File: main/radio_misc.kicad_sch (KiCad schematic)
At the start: 23 parts, among them J1301 Transponder, J1302 Conn_01x03, J1303 Conn_01x03, J1304 Conn_01x03, J1305 Conn_01x03, J1306 Conn_01x03, J1307 Conn_01x03, J1308 USB_B_Micro, M1301 Servo direction, Q1301 IRLML0030, U1301 FT230XQ

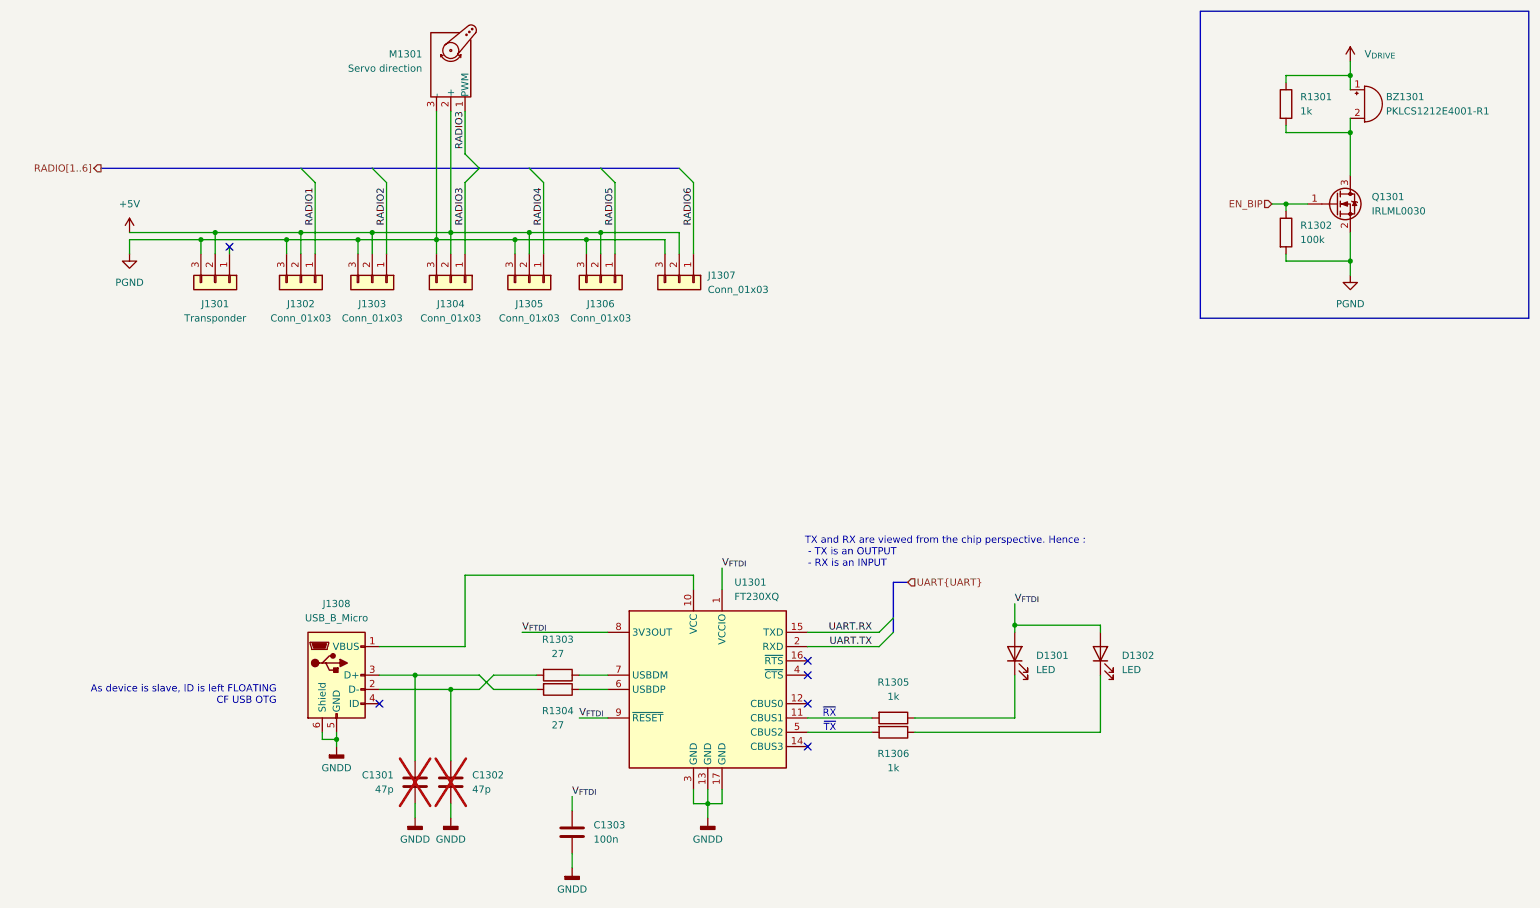
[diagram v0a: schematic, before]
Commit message: Clean silkscreen
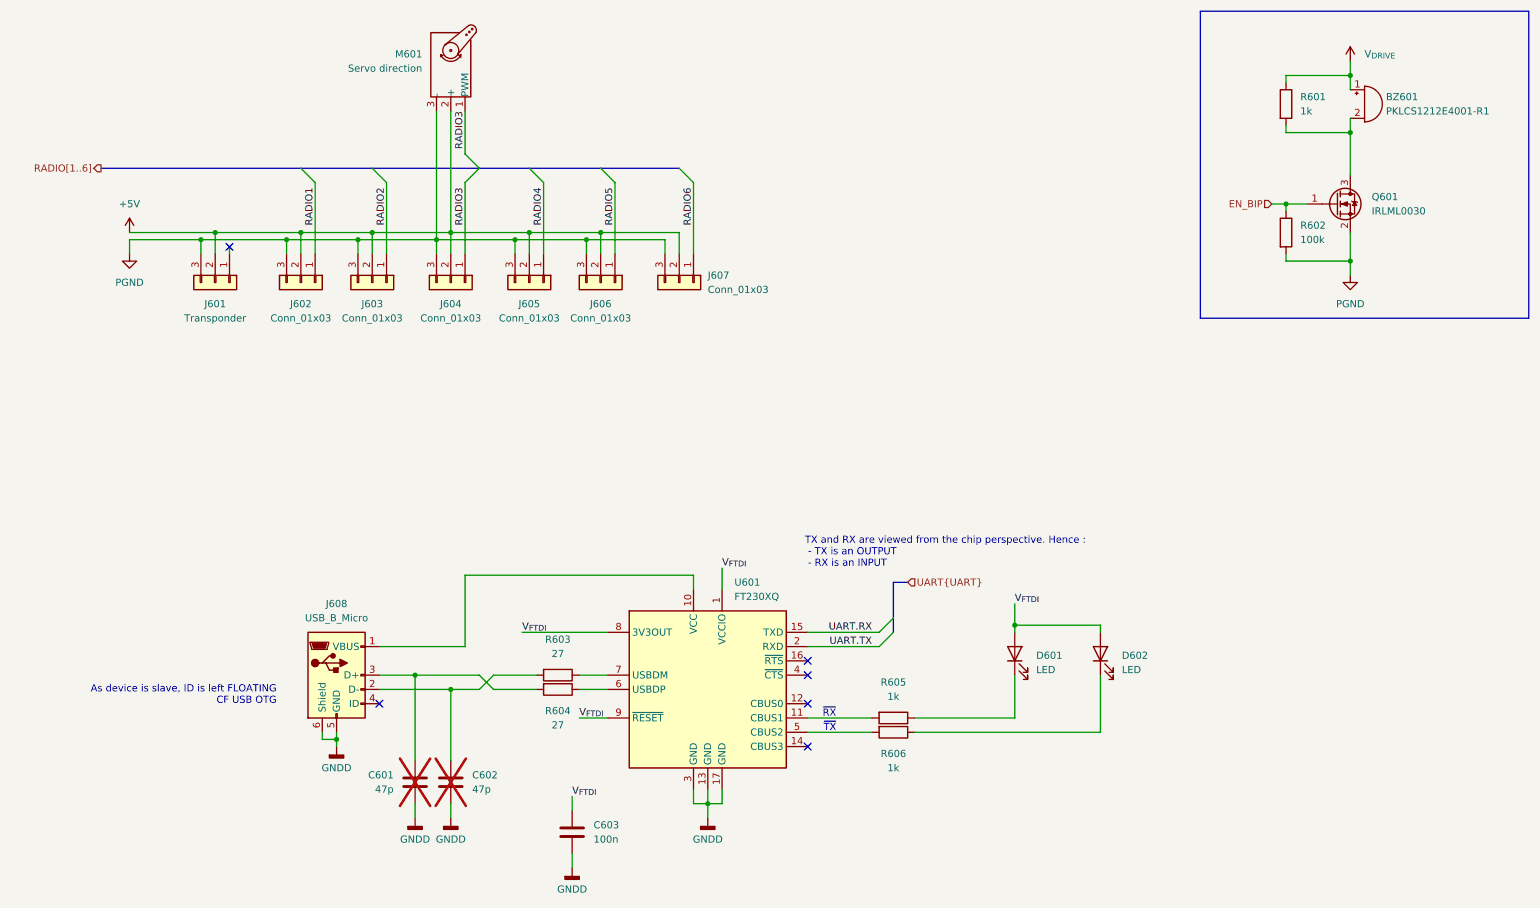
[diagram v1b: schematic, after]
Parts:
- renumbered BZ1301 to BZ601, C1301 to C601, C1302 to C602, C1303 to C603, D1301 to D601, D1302 to D602, J1301 to J601, J1302 to J602, J1303 to J603, J1304 to J604, J1305 to J605, J1306 to J606, J1307 to J607, J1308 to J608, M1301 to M601, Q1301 to Q601, R1301 to R601, R1302 to R602, R1303 to R603, R1304 to R604, R1305 to R605, R1306 to R606, U1301 to U601

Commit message: Sent to fab
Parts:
- C603: MPN (none) -> CL21B104KACNFNC; Mouser SKU (none) -> 187-CL21B104KACNFNC
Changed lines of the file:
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@@
+			)
+		)
+		(property "Quantity" ""
+			(at 240.03 29.21 0)
+			(effects
+				(font
+					(size 1.27 1.27)
+				)
 			)
 		)
@@
 			)
 		)
+		(property "Quantity" ""
+			(at 132.08 60.96 0)
+			(effects
+				(font
+					(size 1.27 1.27)
+				)
+			)
+		)
 		(pin "3"
 		)
@@
 			)
 		)
+		(property "Quantity" ""
+			(at 105.41 60.96 0)
+			(effects
+				(font
+					(size 1.27 1.27)
+				)
+			)
+		)
 		(pin "3"
 		)
@@
 			)
 		)
+		(property "MPN" "CL21B104KACNFNC "
+			(at 113.03 158.75 0)
+			(effects
+				(font
+					(size 1.27 1.27)
+				)
+			)
+		)
+		(property "Mouser SKU" " 187-CL21B104KACNFNC "
+			(at 113.03 158.75 0)
+			(effects
+				(font
+					(size 1.27 1.27)
+				)
+			)
+		)
+		(property "Quantity" ""
+			(at 113.03 158.75 0)
+			(effects
+				(font
+					(size 1.27 1.27)
+				)
+			)
+		)
 		(pin "1"
 		)
@@
 			)
 		)
+		(property "Quantity" ""
+			(at 77.47 60.96 0)
+			(effects
+				(font
+					(size 1.27 1.27)
+				)
+			)
+		)
 		(pin "3"
 		)
@@
 			)
 		)
+		(property "Quantity" ""
+			(at 110.49 133.35 0)
+			(effects
+				(font
+					(size 1.27 1.27)
+				)
+			)
+		)
 		(pin "2"
 		)
@@
 			)
 		)
+		(property "Quantity" ""
+			(at 170.18 138.43 0)
+			(effects
+				(font
+					(size 1.27 1.27)
+				)
+			)
+		)
 		(pin "2"
 		)
@@
 			)
 		)
+		(property "Quantity" ""
+			(at 254 29.21 0)
+			(effects
+				(font
+					(size 1.27 1.27)
+				)
+			)
+		)
 		(pin "2"
 		)
@@
 			)
 		)
+		(property "Quantity" ""
+			(at 248.92 46.99 0)
+			(effects
+				(font
+					(size 1.27 1.27)
+				)
+			)
+		)
 		(pin "3"
 		)
@@
 			)
 		)
+		(property "Quantity" ""
+			(at 64.77 60.96 0)
+			(effects
+				(font
+					(size 1.27 1.27)
+				)
+			)
+		)
 		(pin "3"
 		)
@@
 			)
 		)
+		(property "Quantity" ""
+			(at 137.16 133.35 0)
+			(effects
+				(font
+					(size 1.27 1.27)
+				)
+			)
+		)
 		(pin "17"
 		)
@@
 			)
 		)
+		(property "Quantity" ""
+			(at 91.44 60.96 0)
+			(effects
+				(font
+					(size 1.27 1.27)
+				)
+			)
+		)
 		(pin "3"
 		)
@@
 			)
 		)
+		(property "Quantity" ""
+			(at 170.18 140.97 0)
+			(effects
+				(font
+					(size 1.27 1.27)
+				)
+			)
+		)
 		(pin "2"
 		)
@@
 			)
 		)
+		(property "Quantity" ""
+			(at 118.11 60.96 0)
+			(effects
+				(font
+					(size 1.27 1.27)
+				)
+			)
+		)
 		(pin "3"
 		)
@@
 			)
 		)
+		(property "Quantity" ""
+			(at 110.49 130.81 0)
+			(effects
+				(font
+					(size 1.27 1.27)
+				)
+			)
+		)
 		(pin "2"
 		)
@@
 				)
 				(hide yes)
+			)
+		)
+		(property "Quantity" ""
+			(at 191.77 127 0)
+			(effects
+				(font
+					(size 1.27 1.27)
+				)
 			)
 		)
@@
 			)
 		)
+		(property "Quantity" ""
+			(at 91.44 22.86 0)
+			(effects
+				(font
+					(size 1.27 1.27)
+				)
+			)
+		)
 		(pin "1"
 		)
@@
 			)
 		)
+		(property "Quantity" ""
+			(at 49.53 60.96 0)
+			(effects
+				(font
+					(size 1.27 1.27)
+				)
+			)
+		)
 		(pin "3"
 		)
@@
 			)
 		)
+		(property "Quantity" ""
+			(at 85.09 149.86 0)
+			(effects
+				(font
+					(size 1.27 1.27)
+				)
+			)
+		)
 		(pin "1"
 		)
@@
 			)
 		)
+		(property "Quantity" ""
+			(at 71.12 130.81 0)
+			(effects
+				(font
+					(size 1.27 1.27)
+				)
+			)
+		)
 		(pin "5"
 		)
@@
 			)
 		)
+		(property "Quantity" ""
+			(at 91.44 149.86 0)
+			(effects
+				(font
+					(size 1.27 1.27)
+				)
+			)
+		)
 		(pin "1"
 		)
@@
 			)
 		)
+		(property "Quantity" ""
+			(at 240.03 52.07 0)
+			(effects
+				(font
+					(size 1.27 1.27)
+				)
+			)
+		)
 		(pin "2"
 		)
@@
 			)
 		)
+		(property "Quantity" ""
+			(at 207.01 127 0)
+			(effects
+				(font
+					(size 1.27 1.27)
+				)
+			)
+		)

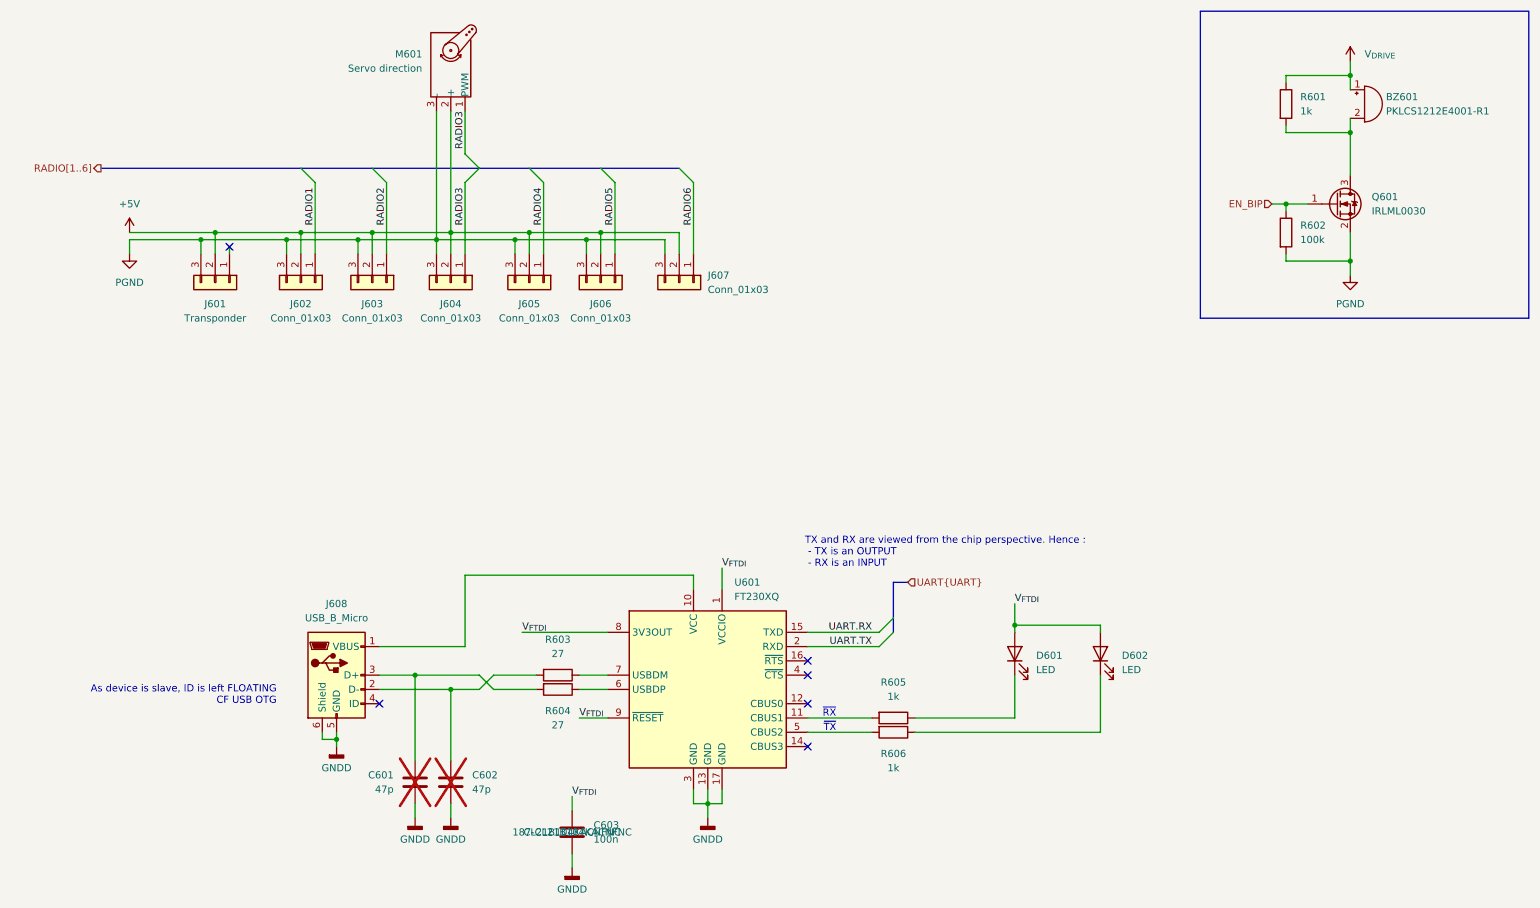
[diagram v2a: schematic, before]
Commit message: BOM almost OK, starts new side board.
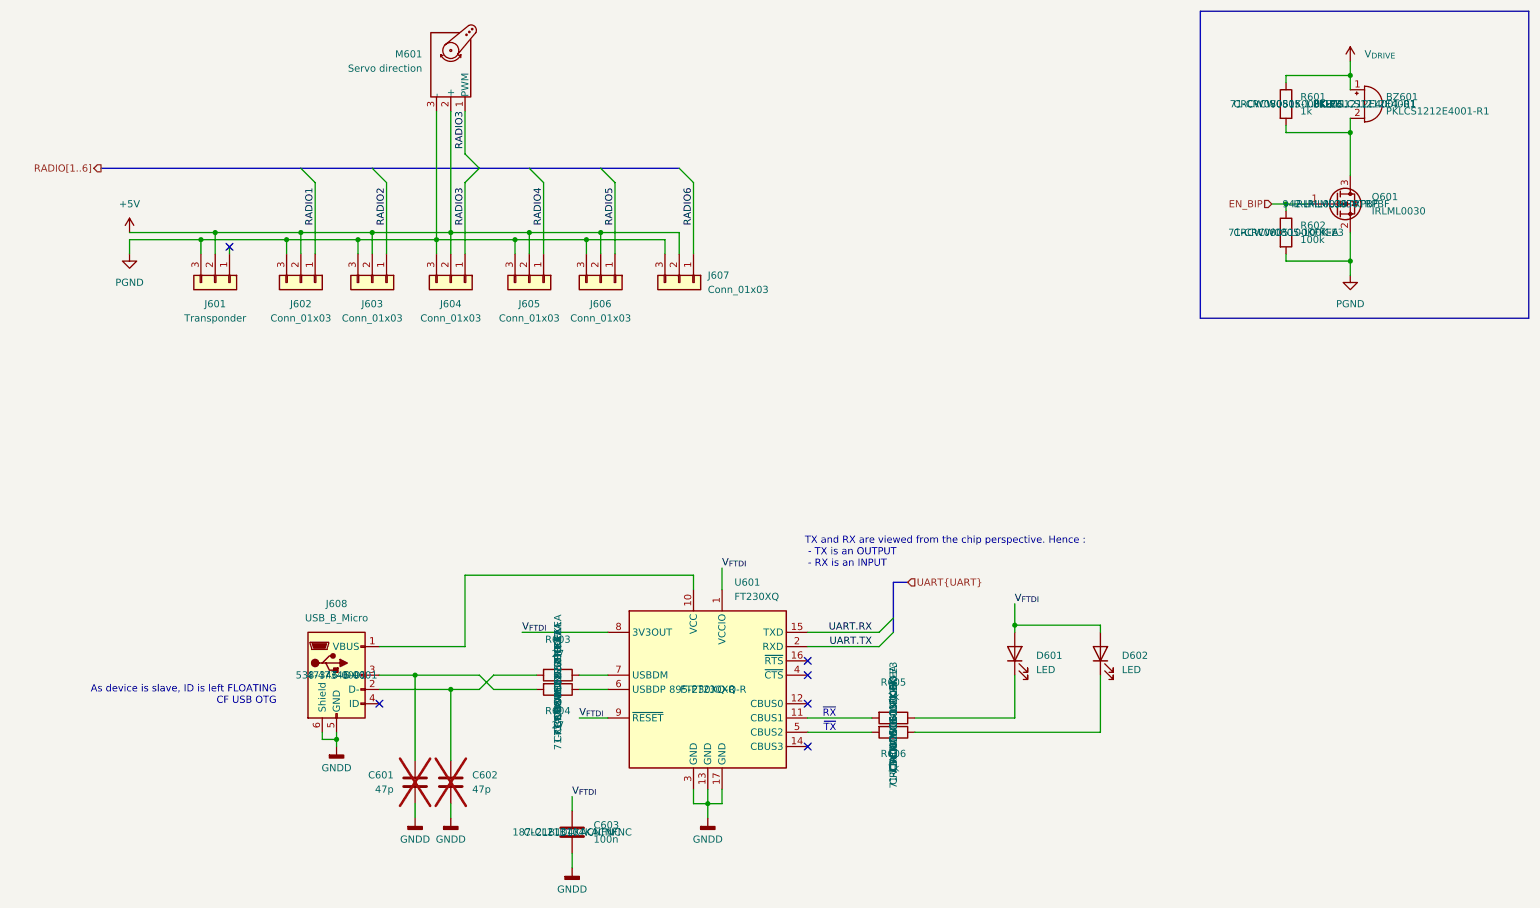
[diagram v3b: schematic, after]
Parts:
- BZ601: MPN (none) -> PKLCS1212E4001-R1; Mouser SKU (none) -> 81-PKLCS1212E4001
- J608: MPN (none) -> 47346-0001; Mouser SKU (none) -> 538-47346-0001
- Q601: MPN (none) -> IRLML0030TRPBF; Mouser SKU (none) -> 942-IRLML0030TRPBF
- R601, R605, R606: MPN (none) -> CRCW08051K00FKEA; Mouser SKU (none) -> 71-CRCW0805-1.0K-E3
- R602: MPN (none) -> CRCW0805100KFKEA; Mouser SKU (none) -> 71-CRCW0805-100K-E3
- R603, R604: MPN (none) -> CRCW080527R0FKEA; Mouser SKU (none) -> 71-CRCW080527R0FKEA
- U601: MPN (none) -> FT230XQ-R; Mouser SKU (none) -> 895-FT230XQ-R
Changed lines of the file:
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@@
 (kicad_sch
-	(version 20240101)
+	(version 20240417)
 	(generator "eeschema")
 	(generator_version "8.99")
@@
 			)
 		)
+		(property "MPN" "CRCW08051K00FKEA"
+			(at 240.03 29.21 0)
+			(effects
+				(font
+					(size 1.27 1.27)
+				)
+			)
+		)
+		(property "Mouser SKU" " 71-CRCW0805-1.0K-E3 "
+			(at 240.03 29.21 0)
+			(effects
+				(font
+					(size 1.27 1.27)
+				)
+			)
+		)
 		(pin "2"
 		)
@@
 			)
 		)
+		(property "MPN" "CRCW080527R0FKEA"
+			(at 110.49 133.35 0)
+			(effects
+				(font
+					(size 1.27 1.27)
+				)
+			)
+		)
+		(property "Mouser SKU" " 71-CRCW080527R0FKEA "
+			(at 110.49 133.35 0)
+			(effects
+				(font
+					(size 1.27 1.27)
+				)
+			)
+		)
 		(pin "2"
 		)
@@
 			)
 		)
+		(property "MPN" "CRCW08051K00FKEA"
+			(at 170.18 138.43 0)
+			(effects
+				(font
+					(size 1.27 1.27)
+				)
+			)
+		)
+		(property "Mouser SKU" " 71-CRCW0805-1.0K-E3 "
+			(at 170.18 138.43 0)
+			(effects
+				(font
+					(size 1.27 1.27)
+				)
+			)
+		)
 		(pin "2"
 		)
@@
 			)
 		)
-		(property "MPN" ""
+		(property "MPN" " PKLCS1212E4001-R1 "
 			(at 254 29.21 0)
 			(effects
@@
 			)
 		)
+		(property "Mouser SKU" " 81-PKLCS1212E4001 "
+			(at 254 29.21 0)
+			(effects
+				(font
+					(size 1.27 1.27)
+				)
+			)
+		)
 		(pin "2"
 		)
@@
 			)
 		)
+		(property "MPN" "IRLML0030TRPBF"
+			(at 248.92 46.99 0)
+			(effects
+				(font
+					(size 1.27 1.27)
+				)
+			)
+		)
+		(property "Mouser SKU" "942-IRLML0030TRPBF "
+			(at 248.92 46.99 0)
+			(effects
+				(font
+					(size 1.27 1.27)
+				)
+			)
+		)
 		(pin "3"
 		)
@@
 			)
 		)
-		(property "MPN" ""
+		(property "MPN" " FT230XQ-R "
 			(at 137.16 133.35 0)
 			(effects
@@
 			)
 		)
+		(property "Mouser SKU" "895-FT230XQ-R "
+			(at 137.16 133.35 0)
+			(effects
+				(font
+					(size 1.27 1.27)
+				)
+			)
+		)
 		(pin "17"
 		)
@@
 			)
 		)
+		(property "MPN" "CRCW08051K00FKEA"
+			(at 170.18 140.97 0)
+			(effects
+				(font
+					(size 1.27 1.27)
+				)
+			)
+		)
+		(property "Mouser SKU" " 71-CRCW0805-1.0K-E3 "
+			(at 170.18 140.97 0)
+			(effects
+				(font
+					(size 1.27 1.27)
+				)
+			)
+		)
 		(pin "2"
 		)
@@
 			)
 		)
+		(property "MPN" "CRCW080527R0FKEA"
+			(at 110.49 130.81 0)
+			(effects
+				(font
+					(size 1.27 1.27)
+				)
+			)
+		)
+		(property "Mouser SKU" " 71-CRCW080527R0FKEA "
+			(at 110.49 130.81 0)
+			(effects
+				(font
+					(size 1.27 1.27)
+				)
+			)
+		)
 		(pin "2"
 		)
@@
 			)
 		)
+		(property "MPN" " 47346-0001"
+			(at 71.12 130.81 0)
+			(effects
+				(font
+					(size 1.27 1.27)
+				)
+			)
+		)
+		(property "Mouser SKU" " 538-47346-0001 "
+			(at 71.12 130.81 0)
+			(effects
+				(font
+					(size 1.27 1.27)
+				)
+			)
+		)
 		(pin "5"
 		)
@@
 			(at 240.03 52.07 0)
 			(effects
+				(font
+					(size 1.27 1.27)
+				)
+			)
+		)
+		(property "MPN" "CRCW0805100KFKEA"
+			(at 240.03 52.07 0)
+			(effects
+				(font
+					(size 1.27 1.27)
+				)
+			)
+		)
+		(property "Mouser SKU" " 71-CRCW0805-100K-E3 "
+			(at 240.03 52.07 0)
+			(effects

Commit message: Revised with BOM ordered
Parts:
- BZ601: MPN PKLCS1212E4001-R1 -> PKLCS1212E4001-R1
- C603: Mouser SKU 187-CL21B104KACNFNC -> 187-CL21B104KACNFNC
- R603, R604: Mouser SKU 71-CRCW080527R0FKEA -> 71-CRCW080527R0FKEA
- U601: MPN FT230XQ-R -> FT230XQ-R
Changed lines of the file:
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@@
 			)
 		)
-		(property "Mouser SKU" " 187-CL21B104KACNFNC "
+		(property "Mouser SKU" "187-CL21B104KACNFNC "
 			(at 113.03 158.75 0)
 			(effects
@@
 			)
 		)
-		(property "Mouser SKU" " 71-CRCW080527R0FKEA "
+		(property "Mouser SKU" "71-CRCW080527R0FKEA "
 			(at 110.49 133.35 0)
 			(effects
@@
 			)
 		)
-		(property "MPN" " PKLCS1212E4001-R1 "
+		(property "MPN" "PKLCS1212E4001-R1 "
 			(at 254 29.21 0)
 			(effects
@@
 			)
 		)
-		(property "MPN" " FT230XQ-R "
+		(property "MPN" "FT230XQ-R "
 			(at 137.16 133.35 0)
 			(effects
@@
 			)
 		)
-		(property "Mouser SKU" " 71-CRCW080527R0FKEA "
+		(property "Mouser SKU" "71-CRCW080527R0FKEA "
 			(at 110.49 130.81 0)
 			(effects
